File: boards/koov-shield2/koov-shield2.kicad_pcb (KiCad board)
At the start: 2 copper layers, 68.6 x 53.3 mm, 31 parts, among them J1 Power, J2 Digital/PWM, J3 Analog, J4 Digital/PWM, SW1 SW_DPDT, U1 DRV8835DSSR

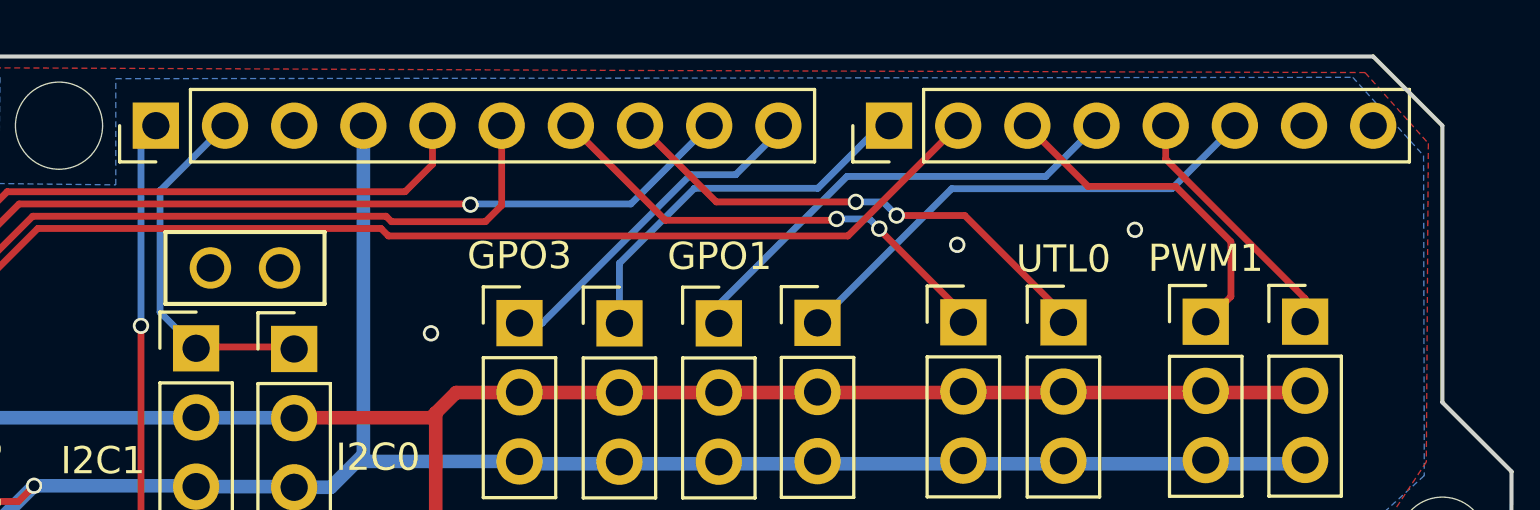
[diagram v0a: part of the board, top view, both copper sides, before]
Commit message: Wiring UARTs to the unused connector.
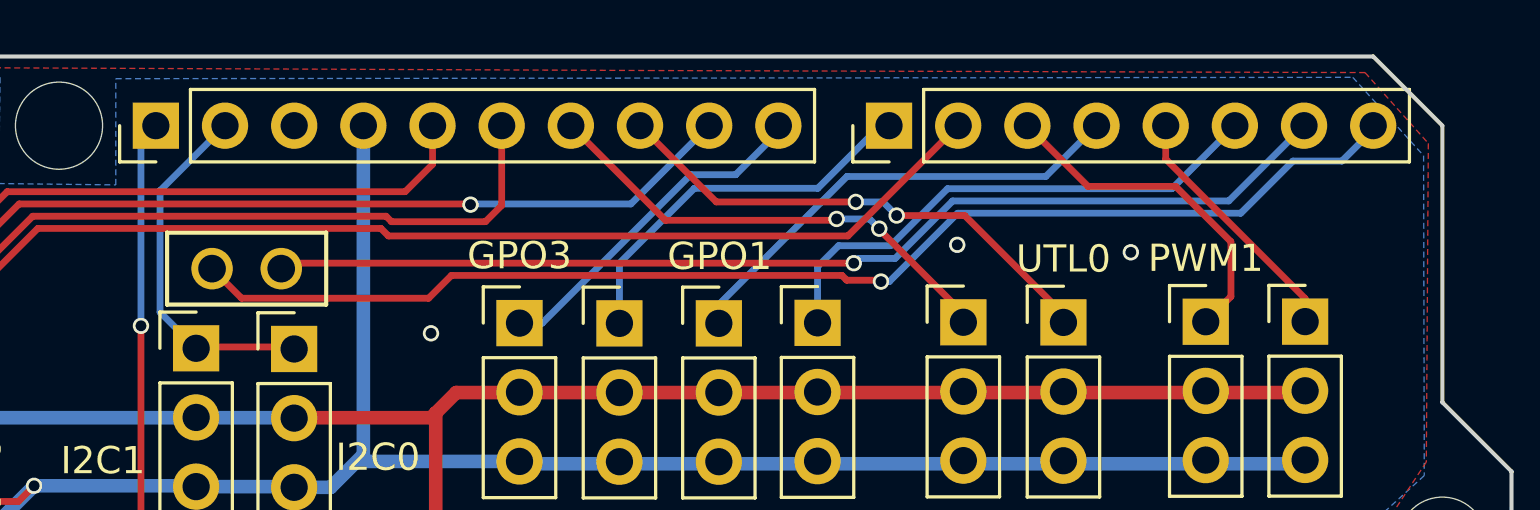
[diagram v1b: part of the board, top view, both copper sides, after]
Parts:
- removed REF**: CONN_RS1-02-G_ADM, Connector:CONN_RS1-02-G_ADM
- added J5: RS1-02-G, Connector:CONN_RS1-02-G_ADM, F.Cu at (120.9, 54.5)
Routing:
- net /0: track 0.00 -> 46.0 mm, vias 0 -> 1
- net /1: track 0.00 -> 39.9 mm, vias 0 -> 1
- net /2: track 18.3 -> 19.5 mm

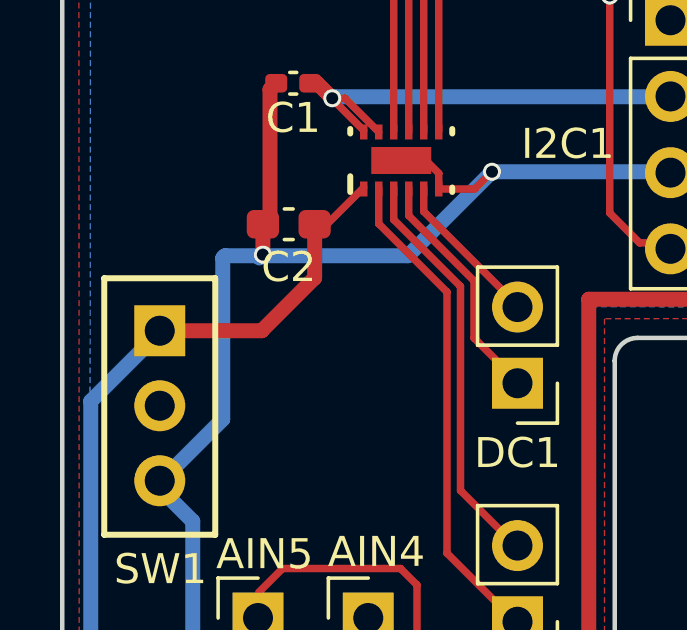
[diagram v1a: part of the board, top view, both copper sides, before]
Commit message: fix swirch miss.
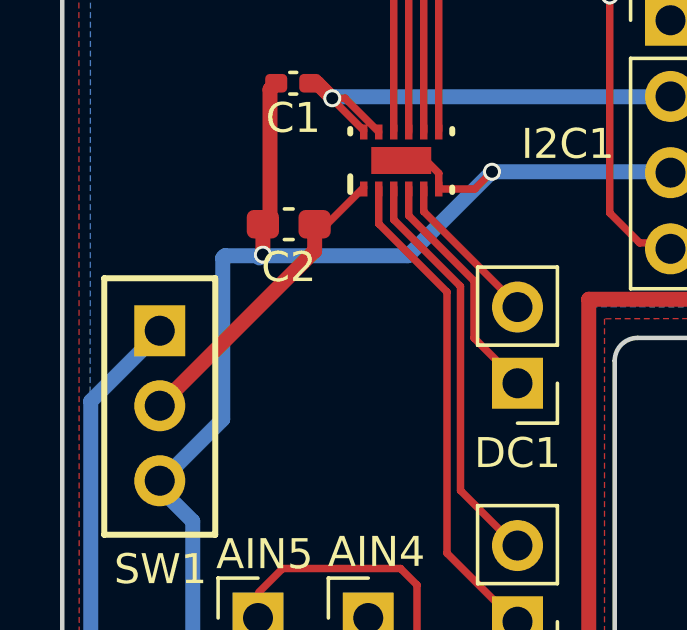
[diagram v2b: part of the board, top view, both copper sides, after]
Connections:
- C2 pad 1: +5V -> /DV_VDD
- U1 pad 1: +5V -> /DV_VDD
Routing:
- net /DV_VDD: track 0.00 -> 10.3 mm
- net +5V: track 76.1 -> 66.4 mm
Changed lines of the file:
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@@
 			(size 0.249999 0.499999)
 			(layers "F.Cu" "F.Paste" "F.Mask")
-			(net 3 "+5V")
+			(net 35 "/DV_VDD")
 			(pinfunction "VM")
 			(pintype "power_in")
@@
 			(layers "F.Cu" "F.Paste" "F.Mask")
 			(roundrect_rratio 0.25)
-			(net 3 "+5V")
+			(net 35 "/DV_VDD")
 			(pintype "passive")
 		)
@@
 	)
 	(segment
-		(start 106.65 67.725)
-		(end 108.4125 65.9625)
-		(width 0.5)
-		(layer "F.Cu")
-		(net 3)
-	)
-	(segment
 		(start 103.25 67.725)
-		(end 106.65 67.725)
+		(end 103.3 67.775)
 		(width 0.5)
 		(layer "F.Cu")
@@
 	)
 	(segment
-		(start 108.4125 64.175)
-		(end 108.824999 64.175)
-		(width 0.25)
-		(layer "F.Cu")
-		(net 3)
-	)
-	(segment
-		(start 108.4125 65.9625)
-		(end 108.4125 64.175)
-		(width 0.5)
-		(layer "F.Cu")
-		(net 3)
-	)
-	(segment
-		(start 108.824999 64.175)
-		(end 110.05 62.949999)
-		(width 0.25)
-		(layer "F.Cu")
-		(net 3)
-	)
-	(segment
 		(start 100.95 95.175)
 		(end 100.95 70.075)
@@
 		(net 34)
 	)
+	(segment
+		(start 103.25 70.225)
+		(end 108.4125 65.0625)
+		(width 0.5)
+		(layer "F.Cu")
+		(net 35)
+	)
+	(segment
+		(start 108.4125 64.175)
+		(end 108.824999 64.175)
+		(width 0.25)
+		(layer "F.Cu")
+		(net 35)
+	)
+	(segment
+		(start 108.4125 65.0625)
+		(end 108.4125 64.175)
+		(width 0.5)
+		(layer "F.Cu")
+		(net 35)
+	)
+	(segment
+		(start 108.824999 64.175)
+		(end 110.05 62.949999)
+		(width 0.25)
+		(layer "F.Cu")
+		(net 35)
+	)
 	(zone
